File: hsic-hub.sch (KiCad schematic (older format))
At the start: 1 part

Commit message: Updated schematics
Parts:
- added C?: C, symbol Device:C
- added R?: 12k, symbol Device:R
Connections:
- net GND: now also R?.2
- net ~HUB_RESET: now reaches U?.12 (~RST)
- net HUB_CONNECT: now reaches U?.2 (HUB_CONNECT)
- net at U?.30 (RBIAS): now also R?.1
- net ~HUB_INT: now reaches U?.5 (~INT)
- net HUB_I2C_SDA: now reaches U?.7 (SDA)
- net HUB_I2C_SCL: now reaches U?.8 (SCL)
- net HSIC_DATA renamed HUB_HSIC_DATA
- net HSIC_STROBE renamed HUB_HSIC_STROBE
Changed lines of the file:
@@
 $Descr A4 11693 8268
 encoding utf-8
-Sheet 3 3
+Sheet 2 2
 Title ""
 Date ""
@@
 	1800 2100 2450 2100
 Text HLabel 1800 2200 0    50   BiDi ~ 0
-HSIC_STROBE
+HUB_HSIC_STROBE
 Text HLabel 1800 2100 0    50   BiDi ~ 0
-HSIC_DATA
+HUB_HSIC_DATA
 $Comp
 L Drone:USB3503 U?
@@
 Wire Wire Line
 	2450 1200 2200 1200
-Text HLabel 950  900  0    50   Input ~ 0
+Text HLabel 1400 850  0    50   Input ~ 0
 3V3
-Text HLabel 950  800  0    50   Input ~ 0
+Text HLabel 1400 750  0    50   Input ~ 0
 GND
-Text Label 1300 800  2    50   ~ 0
+Text Label 1750 750  2    50   ~ 0
 GND
-Text Label 1300 900  2    50   ~ 0
+Text Label 1750 850  2    50   ~ 0
 3V3
 Wire Wire Line
-	950  800  1300 800
+	1400 750  1750 750
 Wire Wire Line
-	1300 900  950  900
+	1750 850  1400 850
+Wire Wire Line
+	1800 2450 2450 2450
+Wire Wire Line
+	1800 2350 2450 2350
+Text HLabel 1800 2450 0    50   BiDi ~ 0
+HUB_I2C_SDA
+Text HLabel 1800 2350 0    50   BiDi ~ 0
+HUB_I2C_SCL
+Wire Wire Line
+	1800 2650 2450 2650
+Wire Wire Line
+	1800 2550 2450 2550
+Text HLabel 1800 2650 0    50   BiDi ~ 0
+~HUB_RESET
+Text HLabel 1800 2550 0    50   BiDi ~ 0
+~HUB_INT
+Wire Wire Line
+	1800 3300 2450 3300
+Text HLabel 1800 3300 0    50   BiDi ~ 0
+HUB_CONNECT
+$Comp
+L Device:C C?
+U 1 1 5E328065
+P 1000 3900
+F 0 "C?" H 1115 3946 50  0000 L CNN
+F 1 "C" H 1115 3855 50  0000 L CNN
+F 2 "" H 1038 3750 50  0001 C CNN
+F 3 "~" H 1000 3900 50  0001 C CNN
+	1    1000 3900
+	1    0    0    -1
+$EndComp
+$Comp
+L Device:R R?
+U 1 1 5E32A1DA
+P 2250 3800
+F 0 "R?" H 2320 3846 50  0000 L CNN
+F 1 "12k" H 2320 3755 50  0000 L CNN
+F 2 "" V 2180 3800 50  0001 C CNN
+F 3 "~" H 2250 3800 50  0001 C CNN
+	1    2250 3800
+	1    0    0    -1
+$EndComp
+Wire Wire Line
+	2450 3150 2250 3150
+Wire Wire Line
+	2250 3150 2250 3650
+Text Label 2250 4150 1    50   ~ 0
+GND
+Wire Wire Line
+	2250 3950 2250 4150
 $EndSCHEMATC

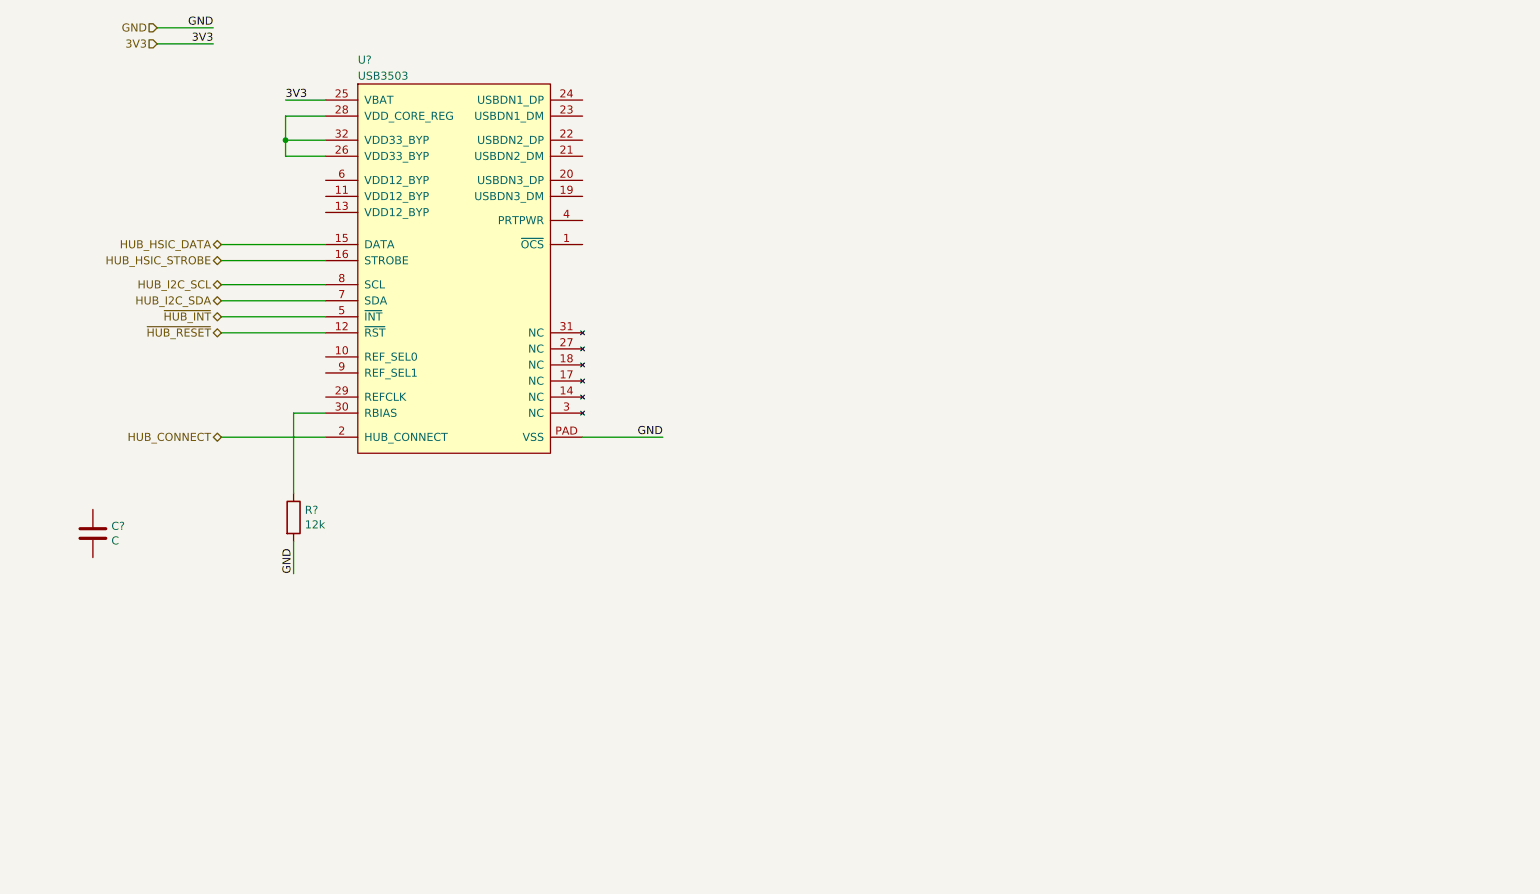
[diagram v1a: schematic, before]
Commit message: connected the USB3503 to the TPS2044 switch (incomplete)
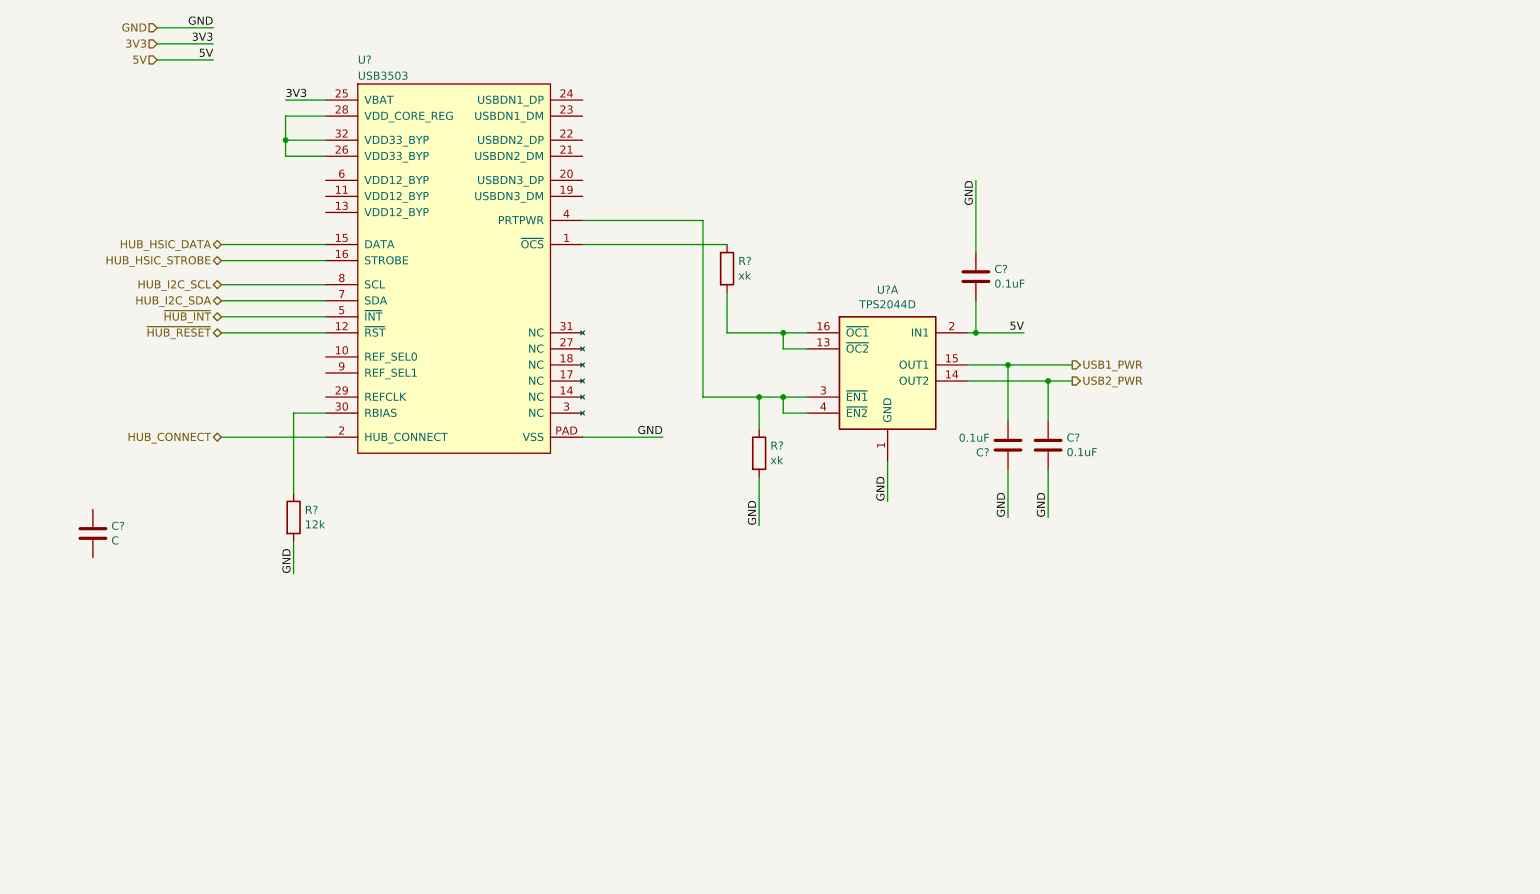
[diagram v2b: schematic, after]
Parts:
- added C? (x3): 0.1uF, symbol Device:C
- added R? (x2): xk, symbol Device:R
- added U?: TPS2044D, Package_SO:SOIC-16_3.9x9.9mm_P1.27mm, symbol Power_Management:TPS2044D
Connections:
- net GND: now also C?.1, C?.1, C?.2, R?.2, U?.1 (GND)
- net at U?.1 (~OCS): now also R?.1
- net at U?.4 (PRTPWR): now also R?.1, U?.3 (~EN1), U?.4 (~EN2)
- new net: R?.2, U?.13 (~OC2), U?.16 (~OC1)
- new net 5V: C?.2, U?.2 (IN1)
- new net USB1_PWR: C?.2, U?.15 (OUT1)
- new net USB2_PWR: C?.1, U?.14 (OUT2)
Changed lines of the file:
@@
 Wire Wire Line
 	2250 3950 2250 4150
+Text HLabel 1400 950  0    50   Input ~ 0
+5V
+Text Label 1750 950  2    50   ~ 0
+5V
+Wire Wire Line
+	1400 950  1750 950
+Wire Wire Line
+	6800 2650 6500 2650
+Text Label 6800 2650 2    50   ~ 0
+5V
+Wire Wire Line
+	5950 3450 5950 3700
+$Comp
+L Power_Management:TPS2044D U?
+U 1 1 5E2F622E
+P 5950 2850
+F 0 "U?" H 5950 3317 50  0000 C CNN
+F 1 "TPS2044D" H 5950 3226 50  0000 C CNN
+F 2 "Package_SO:SOIC-16_3.9x9.9mm_P1.27mm" H 5950 3350 50  0001 C CNN
+F 3 "http://www.ti.com/lit/ds/symlink/tps2044.pdf" H 5900 3150 50  0001 C CNN
+	1    5950 2850
+	1    0    0    -1
+$EndComp
+$Comp
+L Device:R R?
+U 1 1 5E301315
+P 4950 2250
+F 0 "R?" H 5020 2296 50  0000 L CNN
+F 1 "xk" H 5020 2205 50  0000 L CNN
+F 2 "" V 4880 2250 50  0001 C CNN
+F 3 "~" H 4950 2250 50  0001 C CNN
+	1    4950 2250
+	1    0    0    -1
+$EndComp
+Text Label 5950 3700 1    50   ~ 0
+GND
+Wire Wire Line
+	4050 2100 4950 2100
+Wire Wire Line
+	4950 2400 4950 2650
+Wire Wire Line
+	4950 2650 5300 2650
+Wire Wire Line
+	5300 2650 5300 2750
+Wire Wire Line
+	5300 2750 5450 2750
+Connection ~ 5300 2650
+Wire Wire Line
+	5300 2650 5450 2650
+Wire Wire Line
+	4050 1950 4800 1950
+Wire Wire Line
+	4800 1950 4800 3050
+Wire Wire Line
+	4800 3050 5150 3050
+Wire Wire Line
+	5450 3150 5300 3150
+Wire Wire Line
+	5300 3150 5300 3050
+Connection ~ 5300 3050
+Wire Wire Line
+	5300 3050 5450 3050
+$Comp
+L Device:R R?
+U 1 1 5E3318D4
+P 5150 3400
+F 0 "R?" H 5220 3446 50  0000 L CNN
+F 1 "xk" H 5220 3355 50  0000 L CNN
+F 2 "" V 5080 3400 50  0001 C CNN
+F 3 "~" H 5150 3400 50  0001 C CNN
+	1    5150 3400
+	1    0    0    -1
+$EndComp
+Wire Wire Line
+	5150 3050 5150 3250
+Connection ~ 5150 3050
+Wire Wire Line
+	5150 3050 5300 3050
+Text Label 5150 3850 1    50   ~ 0
+GND
+Wire Wire Line
+	5150 3550 5150 3850
+$Comp
+L Device:C C?
+U 1 1 5E332CF8
+P 6500 2300
+F 0 "C?" H 6615 2346 50  0000 L CNN
+F 1 "0.1uF" H 6615 2255 50  0000 L CNN
+F 2 "" H 6538 2150 50  0001 C CNN
+F 3 "~" H 6500 2300 50  0001 C CNN
+	1    6500 2300
+	1    0    0    -1
+$EndComp
+Text Label 6500 1700 3    50   ~ 0
+GND
+Wire Wire Line
+	6500 1700 6500 2150
+Wire Wire Line
+	6500 2450 6500 2650
+Connection ~ 6500 2650
+Wire Wire Line
+	6500 2650 6450 2650
+Text HLabel 7100 2850 2    50   Output ~ 0
+USB1_PWR
+Text HLabel 7100 2950 2    50   Output ~ 0
+USB2_PWR
+Wire Wire Line
+	6450 2850 6700 2850
+Wire Wire Line
+	6450 2950 6950 2950
+Text Label 6700 3800 1    50   ~ 0
+GND
+Wire Wire Line
+	6700 3500 6700 3800
+Text Label 6950 3800 1    50   ~ 0
+GND
+Wire Wire Line
+	6950 3500 6950 3800
+Wire Wire Line
+	6950 2950 6950 3200
+Connection ~ 6950 2950
+Wire Wire Line
+	6950 2950 7100 2950
+Wire Wire Line
+	6700 2850 6700 3200
+Connection ~ 6700 2850
+Wire Wire Line
+	6700 2850 7100 2850
+$Comp
+L Device:C C?
+U 1 1 5E3408C5
+P 6950 3350
+F 0 "C?" H 7065 3396 50  0000 L CNN
+F 1 "0.1uF" H 7065 3305 50  0000 L CNN
+F 2 "" H 6988 3200 50  0001 C CNN
+F 3 "~" H 6950 3350 50  0001 C CNN
+	1    6950 3350
+	1    0    0    -1
+$EndComp
+$Comp
+L Device:C C?
+U 1 1 5E340CE5
+P 6700 3350
+F 0 "C?" H 6815 3396 50  0000 L CNN
+F 1 "0.1uF" H 6815 3305 50  0000 L CNN
+F 2 "" H 6738 3200 50  0001 C CNN
+F 3 "~" H 6700 3350 50  0001 C CNN
+	1    6700 3350
+	-1   0    0    1
+$EndComp
 $EndSCHEMATC

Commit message: fixed pull up connection
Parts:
- removed R?: xk, symbol Device:R
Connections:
- net 3V3: now also R?.1
- net at U?.1 (~OCS): now also R?.2, U?.13 (~OC2), U?.16 (~OC1); no longer R?.1
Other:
- moved on the sheet: R?
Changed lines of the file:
@@
 L Device:R R?
 U 1 1 5E301315
-P 4950 2250
-F 0 "R?" H 5020 2296 50  0000 L CNN
-F 1 "xk" H 5020 2205 50  0000 L CNN
-F 2 "" V 4880 2250 50  0001 C CNN
-F 3 "~" H 4950 2250 50  0001 C CNN
-	1    4950 2250
+P 5300 1850
+F 0 "R?" H 5370 1896 50  0000 L CNN
+F 1 "xk" H 5370 1805 50  0000 L CNN
+F 2 "" V 5230 1850 50  0001 C CNN
+F 3 "~" H 5300 1850 50  0001 C CNN
+	1    5300 1850
 	1    0    0    -1
 $EndComp
@@
 Wire Wire Line
 	4050 2100 4950 2100
-Wire Wire Line
-	4950 2400 4950 2650
 Wire Wire Line
 	4950 2650 5300 2650
@@
 	4800 1950 4800 3050
 Wire Wire Line
-	4800 3050 5150 3050
-Wire Wire Line
 	5450 3150 5300 3150
 Wire Wire Line
@@
 Wire Wire Line
 	5300 3050 5450 3050
-$Comp
-L Device:R R?
-U 1 1 5E3318D4
-P 5150 3400
-F 0 "R?" H 5220 3446 50  0000 L CNN
-F 1 "xk" H 5220 3355 50  0000 L CNN
-F 2 "" V 5080 3400 50  0001 C CNN
-F 3 "~" H 5150 3400 50  0001 C CNN
-	1    5150 3400
-	1    0    0    -1
-$EndComp
-Wire Wire Line
-	5150 3050 5150 3250
-Connection ~ 5150 3050
-Wire Wire Line
-	5150 3050 5300 3050
-Text Label 5150 3850 1    50   ~ 0
-GND
-Wire Wire Line
-	5150 3550 5150 3850
 $Comp
 L Device:C C?
@@
 	-1   0    0    1
 $EndComp
+Text Label 5300 1500 3    50   ~ 0
+3V3
+Wire Wire Line
+	5300 1500 5300 1700
+Wire Wire Line
+	5300 2000 5300 2650
+Wire Wire Line
+	4950 2100 4950 2650
+Wire Wire Line
+	4800 3050 5300 3050
 $EndSCHEMATC

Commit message: Add oscillator to HSIC hub circuit
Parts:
- added C?: 1n, symbol Device:C
- added X?: ASTXR-12, Drone:ASTXR-12, symbol Drone:ASTXR-12
- C?: value C -> 100n
- R?: value 12k -> 12k,1%
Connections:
- net 3V3: now also C?.1, X?.6 (VDD)
- net GND: now also C?.2, U?.10 (REF_SEL0), U?.9 (REF_SEL1), X?.3 (GND)
- net REFCLK: now reaches U?.29 (REFCLK)
- net REFCLK: now also C?.1
- new net: C?.2, X?.4 (OUT)
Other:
- note added: "Check datasheet for correct placement\nof bypass and filter capacitors"
- note added: "what is the logic level of all these signals, 1.2V?\nDoes that match the pins on the Up Board?"
- moved on the sheet: C?
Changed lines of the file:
@@
 F 1 "USB3503" H 2650 1150 50  0000 L CNN
 F 2 "" H 3250 1100 50  0001 C CNN
-F 3 "" H 3250 1100 50  0001 C CNN
+F 3 "http://www.microchip.com/mymicrochip/filehandler.aspx?ddocname=en566511" H 3250 1100 50  0001 C CNN
 	1    3250 1100
 	1    0    0    -1
@@
 L Device:C C?
 U 1 1 5E328065
-P 1000 3900
-F 0 "C?" H 1115 3946 50  0000 L CNN
-F 1 "C" H 1115 3855 50  0000 L CNN
-F 2 "" H 1038 3750 50  0001 C CNN
-F 3 "~" H 1000 3900 50  0001 C CNN
-	1    1000 3900
+P 1200 5150
+F 0 "C?" H 1315 5196 50  0000 L CNN
+F 1 "100n" H 1315 5105 50  0000 L CNN
+F 2 "" H 1238 5000 50  0001 C CNN
+F 3 "~" H 1200 5150 50  0001 C CNN
+	1    1200 5150
 	1    0    0    -1
 $EndComp
@@
 P 2250 3800
 F 0 "R?" H 2320 3846 50  0000 L CNN
-F 1 "12k" H 2320 3755 50  0000 L CNN
+F 1 "12k,1%" H 2320 3755 50  0000 L CNN
 F 2 "" V 2180 3800 50  0001 C CNN
 F 3 "~" H 2250 3800 50  0001 C CNN
@@
 Wire Wire Line
 	4800 3050 5300 3050
+$Comp
+L Drone:ASTXR-12 X?
+U 1 1 5E308236
+P 1900 5000
+F 0 "X?" H 1700 5150 50  0000 L CNN
+F 1 "ASTXR-12" H 1700 5050 50  0000 L CNN
+F 2 "Drone:ASTXR-12" H 1700 4650 50  0001 L CNN
+F 3 "https://abracon.com/Oscillators/ASTXR-12-38.400MHz-514054-T.pdf" H 1700 5250 50  0001 L CNN
+	1    1900 5000
+	1    0    0    -1
+$EndComp
+Text Notes 500  2000 0    50   ~ 0
+what is the logic level of all these signals, 1.2V?\nDoes that match the pins on the Up Board?
+Text Label 2950 4750 2    50   ~ 0
+3V3
+Text Label 2950 5450 2    50   ~ 0
+GND
+Text Label 1500 3050 0    50   ~ 0
+REFCLK
+Wire Wire Line
+	2450 3050 1500 3050
+Text Label 2950 5150 2    50   ~ 0
+REFCLK
+Text Label 2150 4150 1    50   ~ 0
+GND
+Text Label 2050 4150 1    50   ~ 0
+GND
+Wire Wire Line
+	2150 4150 2150 2900
+Wire Wire Line
+	2150 2900 2450 2900
+Wire Wire Line
+	2050 4150 2050 2800
+Wire Wire Line
+	2050 2800 2450 2800
+$Comp
+L Device:C C?
+U 1 1 5E338829
+P 2450 5150
+F 0 "C?" H 2565 5196 50  0000 L CNN
+F 1 "1n" H 2565 5105 50  0000 L CNN
+F 2 "" H 2488 5000 50  0001 C CNN
+F 3 "~" H 2450 5150 50  0001 C CNN
+	1    2450 5150
+	0    1    1    0
+$EndComp
+Wire Wire Line
+	2600 5150 2950 5150
+Wire Wire Line
+	2200 5150 2300 5150
+Wire Wire Line
+	2200 5050 2300 5050
+Wire Wire Line
+	2300 5050 2300 4750
+Wire Wire Line
+	1200 4750 1200 5000
+Wire Wire Line
+	1200 5300 1200 5450
+Wire Wire Line
+	1200 5450 2300 5450
+Wire Wire Line
+	2300 5450 2300 5250
+Wire Wire Line
+	2300 5250 2200 5250
+Wire Wire Line
+	2300 4750 1200 4750
+Wire Wire Line
+	2950 5450 2300 5450
+Connection ~ 2300 5450
+Wire Wire Line
+	2950 4750 2300 4750
+Connection ~ 2300 4750
+Text Notes 1300 5750 0    50   ~ 0
+Check datasheet for correct placement\nof bypass and filter capacitors
 $EndSCHEMATC
